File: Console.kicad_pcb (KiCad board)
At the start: 2 copper layers, 59.6 x 60.4 mm, 61 parts, among them J1 batt_in, J11 lcd_out, J14 gnd_out, J17 node_conn_1, J18 node_conn_2, J2 3v3_gnd, J3 motor_out, J4 ir_out, J5 pwr_jumper, J6 gpio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

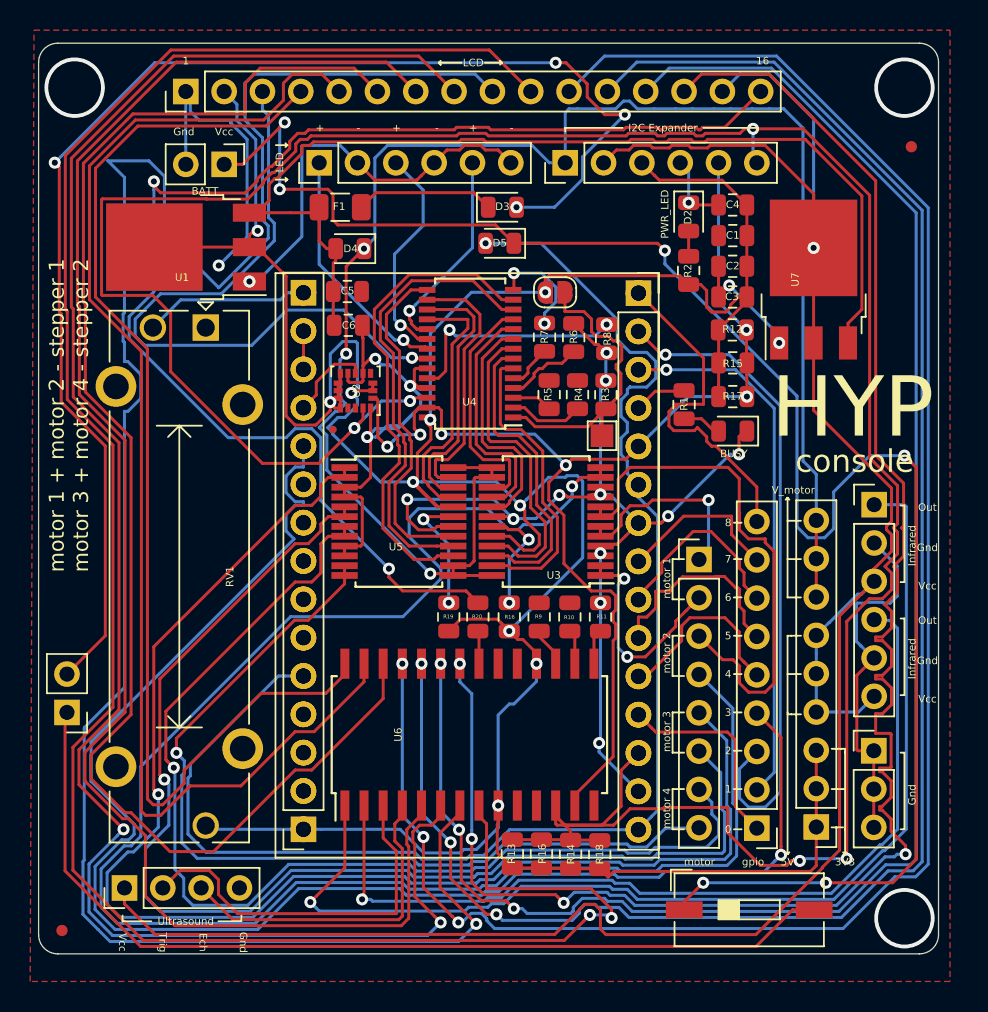
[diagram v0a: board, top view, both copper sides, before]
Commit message: Changed Switch footprint
Changed the switch to SPDT and its footprint to a mouser available switch and made all the legends visible. Added a testpoint for gnd. Final Check yet to be done
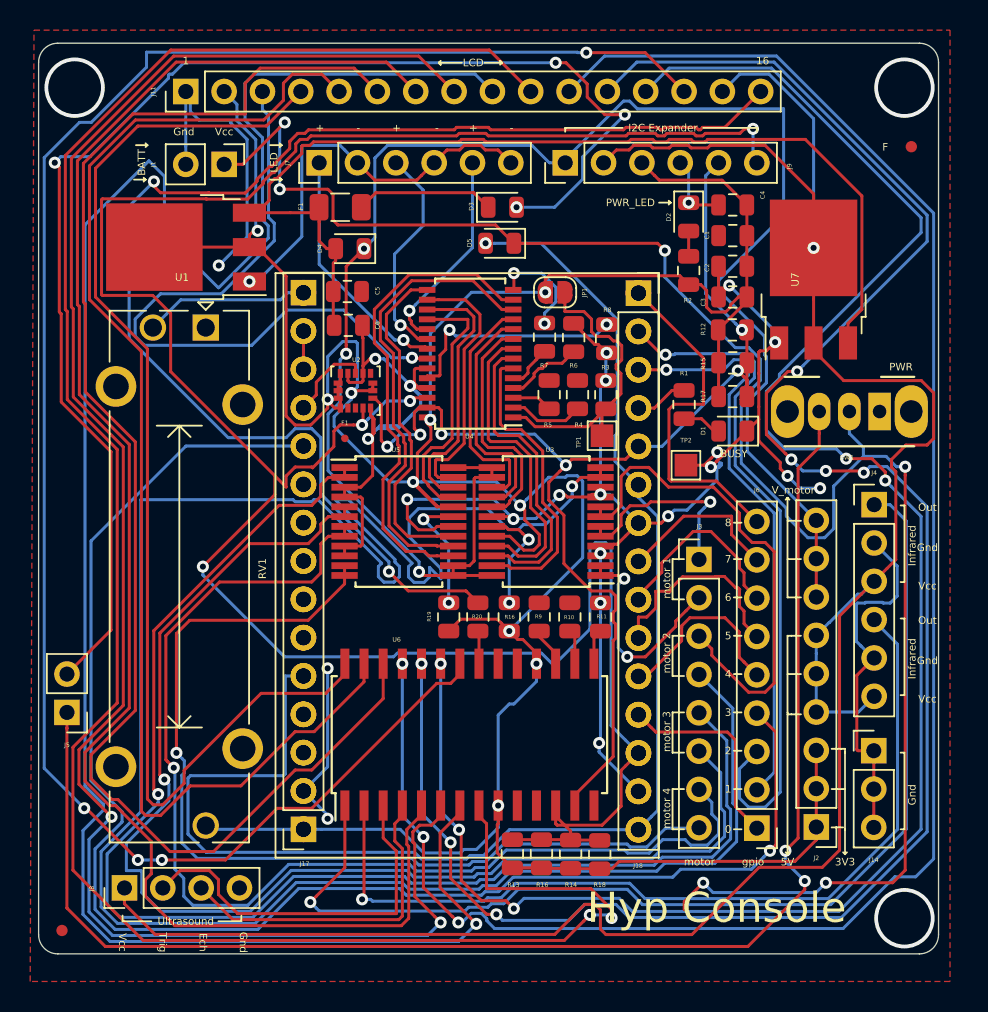
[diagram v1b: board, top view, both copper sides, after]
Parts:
- removed the F at (77.3, 55.4)
- added F1: Fiducial_0.5mm_Mask1mm, Fiducial:Fiducial_0.5mm_Mask1mm, F.Cu at (78.1, 56.0)
- added TP2: TestPoint, TestPoint:TestPoint_Pad_1.5x1.5mm, F.Cu at (100.7, 57.8)
- SW1: value SW_SPST -> SW_SPDT; footprint Button_Switch_SMD:SW_DIP_SPSTx01_Slide_9.78x4.72mm_W8.61mm_P2.54mm -> Button_Switch_THT:SW_CuK_OS102011MA1QN1_SPDT_Angled
- moved SW1 34.1 mm to (113.5, 54.2), turned to 180 degrees
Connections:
- NMCU1 pad D3: /DEF_LED -> /BSY_LED
- R1 pad 2: /DEF_LED -> /BSY_LED
- SW1 pad 1: /SWITCH_IN -> Net-(SW1-Pad1)
- SW1 pad 2: Net-(J5-Pad1) -> /SWITCH_IN
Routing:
- net Net-(J5-Pad1): track 63.3 -> 97.6 mm, vias 0 -> 2
- net /m21: track 114.7 -> 144.9 mm
- net GND: track 199.8 -> 229.4 mm, vias 21 -> 26
- net /SCL: track 184.5 -> 166.2 mm, vias 5 -> 4
- net /LCD_D5: track 118.8 -> 130.9 mm, vias 3 -> 7
- net /LCD_D6: track 113.7 -> 124.1 mm, vias 3 -> 5
- net /LCD_D7: track 115.5 -> 123.3 mm
- net +5V: track 148.3 -> 154.4 mm
- net /SWITCH_IN: track 115.1 -> 120.3 mm
- net /m41: track 59.9 -> 64.0 mm
- net /DEF_LED: track 3.33 -> 0.00 mm
- net /m42: track 73.0 -> 76.2 mm
- net /SDA: track 77.6 -> 80.3 mm
- net +3V3: track 228.2 -> 225.5 mm
- net /LCD_D2: track 135.2 -> 132.4 mm
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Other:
- board text added: "A Product of Tarcin Corporation | tarcin.in | Made in India"
- board text added: "Hyp Console"
- board text added: "PWR"
- board text removed: "A Product of Tarcin Corporation | contact@tarcin.in"
- board text removed: "HYP"
- board text removed: "console"

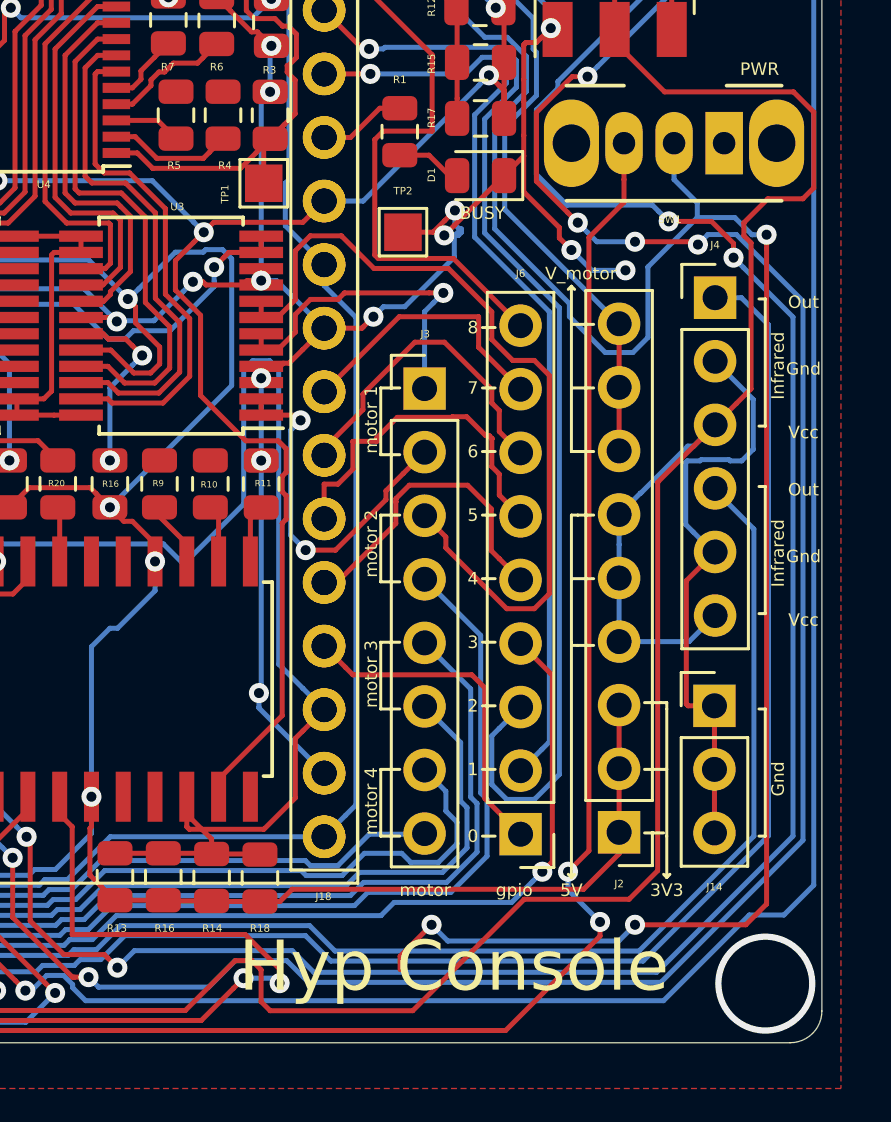
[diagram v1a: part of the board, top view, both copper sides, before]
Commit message: removed residue after modifying the switch
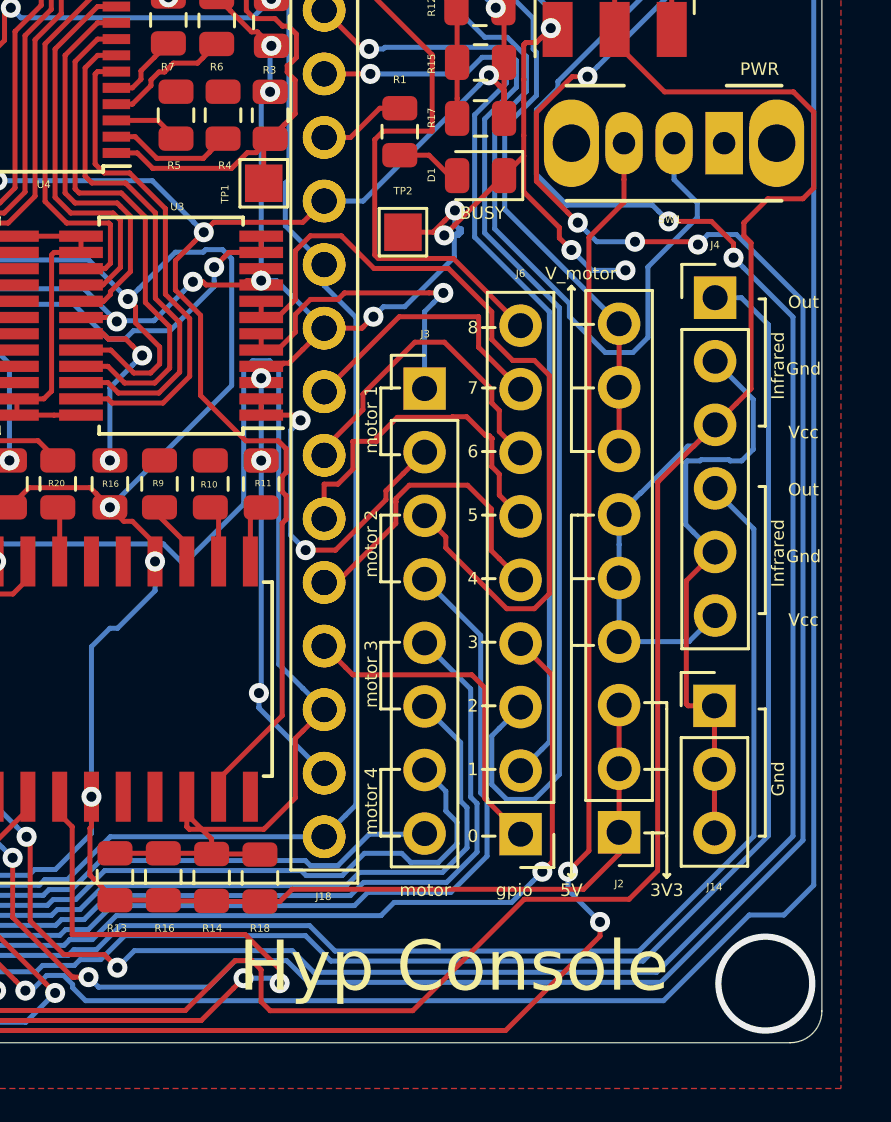
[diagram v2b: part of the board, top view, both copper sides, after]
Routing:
- net /SWITCH_IN: track 120.3 -> 73.9 mm, vias 6 -> 3
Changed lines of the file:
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@@
     (thickness 1.6)
     (drawings 160)
-    (tracks 1841)
+    (tracks 1826)
     (zones 0)
     (modules 62)
@@
   (segment (start 89.3064 43.0784) (end 98.8314 43.0784) (width 0.2) (layer F.Cu) (net 8))
   (segment (start 98.8314 43.0784) (end 99.314 43.561) (width 0.2) (layer F.Cu) (net 8))
-  (via (at 109.982 85.457256) (size 0.8) (drill 0.4) (layers F.Cu B.Cu) (net 8))
-  (via (at 101.854 85.457256) (size 0.8) (drill 0.4) (layers F.Cu B.Cu) (net 8))
-  (segment (start 100.597 86.714256) (end 100.597 87.249) (width 0.2) (layer F.Cu) (net 8))
-  (segment (start 101.854 85.457256) (end 100.597 86.714256) (width 0.2) (layer F.Cu) (net 8))
   (via (at 73.787 39.497) (size 0.8) (drill 0.4) (layers F.Cu B.Cu) (net 8))
   (segment (start 88.09381 41.86581) (end 77.644396 41.86581) (width 0.2) (layer F.Cu) (net 8))
@@
   (segment (start 71.34795 37.846) (end 70.104 37.846) (width 0.2) (layer F.Cu) (net 8))
   (segment (start 74.122923 35.071027) (end 71.34795 37.846) (width 0.2) (layer F.Cu) (net 8))
-  (segment (start 102.502744 86.106) (end 101.854 85.457256) (width 0.2) (layer B.Cu) (net 8))
-  (segment (start 109.333256 86.106) (end 102.502744 86.106) (width 0.2) (layer B.Cu) (net 8))
-  (segment (start 109.982 85.457256) (end 109.333256 86.106) (width 0.2) (layer B.Cu) (net 8))
   (segment (start 107.360023 61.157625) (end 108.794999 62.592601) (width 0.2) (layer B.Cu) (net 8))
   (segment (start 104.374989 53.428311) (end 104.374989 57.650387) (width 0.2) (layer B.Cu) (net 8))
@@
   (segment (start 103.980369 49.996967) (end 104.877969 49.996967) (width 0.2) (layer B.Cu) (net 8))
   (segment (start 99.314 45.330598) (end 103.980369 49.996967) (width 0.2) (layer B.Cu) (net 8))
-  (segment (start 112.470995 57.201005) (end 113.970005 57.201005) (width 0.2) (layer B.Cu) (net 8))
   (segment (start 110.497001 59.174999) (end 112.470995 57.201005) (width 0.2) (layer B.Cu) (net 8))
   (segment (start 108.794999 62.592601) (end 109.899001 62.592601) (width 0.2) (layer B.Cu) (net 8))
@@
   (segment (start 104.877969 49.996967) (end 105.644989 50.763987) (width 0.2) (layer B.Cu) (net 8))
   (segment (start 99.314 43.561) (end 99.314 45.330598) (width 0.2) (layer B.Cu) (net 8))
-  (segment (start 114.409946 85.457256) (end 115.238902 84.6283) (width 0.2) (layer F.Cu) (net 8))
-  (segment (start 115.238902 58.451509) (end 115.238902 57.885824) (width 0.2) (layer F.Cu) (net 8))
-  (segment (start 113.970005 57.201005) (end 114.654824 57.885824) (width 0.2) (layer B.Cu) (net 8))
-  (via (at 115.238902 57.885824) (size 0.8) (drill 0.4) (layers F.Cu B.Cu) (net 8))
-  (segment (start 115.238902 84.6283) (end 115.238902 58.451509) (width 0.2) (layer F.Cu) (net 8))
-  (segment (start 114.673217 57.885824) (end 115.238902 57.885824) (width 0.2) (layer B.Cu) (net 8))
-  (segment (start 114.654824 57.885824) (end 114.673217 57.885824) (width 0.2) (layer B.Cu) (net 8))
-  (segment (start 109.982 85.457256) (end 114.409946 85.457256) (width 0.2) (layer F.Cu) (net 8))
+  (segment (start 111.542 54.229) (end 111.542 54.729) (width 0.2) (layer F.Cu) (net 8))
+  (segment (start 112.470995 56.607995) (end 112.470995 57.201005) (width 0.2) (layer B.Cu) (net 8))
+  (segment (start 111.542 55.679) (end 112.470995 56.607995) (width 0.2) (layer B.Cu) (net 8))
+  (segment (start 111.542 54.229) (end 111.542 55.679) (width 0.2) (layer B.Cu) (net 8))
   (segment (start 86.7718 65.0938) (end 85.2864 65.0938) (width 0.2) (layer F.Cu) (net 9))
   (segment (start 87.8468 65.0938) (end 86.7718 65.0938) (width 0.2) (layer F.Cu) (net 9))
@@
   (segment (start 81.915 81.0412) (end 81.915 80.3412) (width 0.2) (layer F.Cu) (net 33))
   (segment (start 81.415 82.693402) (end 81.415 81.5412) (width 0.2) (layer F.Cu) (net 33))
-  (segment (start 94.846163 54.607437) (end 95.4024 54.0512) (width 0.2) (layer F.Cu) (net 34))
-  (segment (start 94.21948 55.23412) (end 94.846163 54.607437) (width 0.2) (layer F.Cu) (net 34))
-  (segment (start 90.710621 55.23412) (end 94.21948 55.23412) (width 0.2) (layer F.Cu) (net 34))
-  (segment (start 90.095102 54.6186) (end 90.710621 55.23412) (width 0.2) (layer F.Cu) (net 34))
-  (segment (start 89.2608 54.6186) (end 90.095102 54.6186) (width 0.2) (layer F.Cu) (net 34))
   (segment (start 95.1484 54.3052) (end 95.4024 54.0512) (width 0.2) (layer F.Cu) (net 34))
   (segment (start 95.1484 55.8292) (end 95.1484 54.3052) (width 0.2) (layer F.Cu) (net 34))
@@
   (segment (start 96.083884 51.38869) (end 96.40241 51.707216) (width 0.2) (layer F.Cu) (net 34))
   (segment (start 96.40241 53.05119) (end 95.958637 53.494963) (width 0.2) (layer F.Cu) (net 34))
+  (segment (start 94.846163 54.607437) (end 95.4024 54.0512) (width 0.2) (layer F.Cu) (net 34))
+  (segment (start 94.490563 54.607437) (end 94.846163 54.607437) (width 0.2) (layer F.Cu) (net 34))
+  (segment (start 93.86388 55.23412) (end 94.490563 54.607437) (width 0.2) (layer F.Cu) (net 34))
+  (segment (start 90.710621 55.23412) (end 93.86388 55.23412) (width 0.2) (layer F.Cu) (net 34))
+  (segment (start 89.2608 54.6186) (end 90.095102 54.6186) (width 0.2) (layer F.Cu) (net 34))
+  (segment (start 90.095102 54.6186) (end 90.710621 55.23412) (width 0.2) (layer F.Cu) (net 34))
   (segment (start 76.211799 52.280399) (end 77.394199 51.097999) (width 0.2) (layer F.Cu) (net 35))
   (segment (start 77.394199 51.097999) (end 78.724201 51.097999) (width 0.2) (layer F.Cu) (net 35))
@@
   (segment (start 108.585 85.909685) (end 104.813675 89.68101) (width 0.2) (layer F.Cu) (net 94))
   (segment (start 108.585 85.344) (end 108.585 85.909685) (width 0.2) (layer F.Cu) (net 94))
-  (segment (start 111.542 54.229) (end 111.542 54.729) (width 0.2) (layer F.Cu) (net 8))
-  (segment (start 112.470995 56.607995) (end 112.470995 57.201005) (width 0.2) (layer B.Cu) (net 8))
-  (segment (start 111.542 55.679) (end 112.470995 56.607995) (width 0.2) (layer B.Cu) (net 8))
-  (segment (start 111.542 54.229) (end 111.542 55.679) (width 0.2) (layer B.Cu) (net 8))
   (segment (start 109.542 55.679) (end 109.542 54.229) (width 0.2) (layer F.Cu) (net 94))
   (segment (start 109.542 56.594002) (end 109.542 55.679) (width 0.2) (layer F.Cu) (net 94))

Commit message: Updated the board size
Using a pitch of 8mm,the drills were adjusted and the board size was standardized to 64x64
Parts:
- removed the F at (115.6, 36.7)
- removed the F at (59.4, 88.6)
- removed the F1 at (78.1, 56.0)
- removed the F1 at (77.8, 40.7)
- removed the R16 at (91.1, 83.5)
- removed the R16 at (89.0, 67.8)
- added F: Fiducial_0.75mm_Mask2.25mm, Fiducial:Fiducial_0.75mm_Mask2.25mm, F.Cu at (1.42, 66.0)
- added F: Fiducial_0.75mm_Mask2.25mm, Fiducial:Fiducial_0.75mm_Mask2.25mm, F.Cu at (-58.0, 114.7)
- added F1: Fiducial_0.5mm_Mask1mm, Fiducial:Fiducial_0.5mm_Mask1mm, F.Cu at (-37.9, 85.0)
- added F1: Fuse, Fuse:Fuse_1206_3216Metric, F.Cu at (-38.2, 69.7)
- added R16: 10k, Resistor_SMD:R_0805_2012Metric, F.Cu at (-24.9, 112.5)
- added R16: 10k, Resistor_SMD:R_0805_2012Metric, F.Cu at (-27.0, 96.8)
- moved C1 119.6 mm to (-12.2, 71.6)
- moved C2 119.6 mm to (-12.2, 73.6)
- moved C3 119.6 mm to (-12.2, 75.6)
- moved C4 119.6 mm to (-12.2, 69.5)
- moved C5 119.6 mm to (-37.7, 75.3)
- moved C6 119.6 mm to (-37.7, 77.5)
- moved D1 119.6 mm to (-12.2, 84.5)
- moved D2 119.6 mm to (-15.1, 70.3)
- moved D3 119.6 mm to (-27.5, 69.7)
- moved D4 119.6 mm to (-37.6, 72.4)
- moved D5 119.6 mm to (-27.6, 72.1)
- moved J1 119.6 mm to (-45.9, 66.8)
- moved J11 119.6 mm to (-48.4, 62.0)
- moved J14 119.6 mm to (-2.84, 105.7)
- moved J17 119.6 mm to (-40.6, 110.9)
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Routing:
- net /m21: track 144.9 -> 128.6 mm
- net /LCD_D2: track 132.4 -> 142.0 mm
- net /LCD_D1: track 117.3 -> 126.1 mm
- net /LCD_D7: track 123.3 -> 124.1 mm
- net Net-(J5-Pad1): track 97.6 -> 97.0 mm
- net (no net): vias 3 -> 4
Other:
- board size 59.6 x 60.4 mm -> 64 x 64 mm
